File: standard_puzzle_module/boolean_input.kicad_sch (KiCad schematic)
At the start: 6 parts, among them J8 Screw_Terminal_01x02, U8 PC817

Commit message: feat: unscrew git tracking
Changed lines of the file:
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@@
+	(wire
+		(pts
+			(xy 166.37 90.17) (xy 172.72 90.17)
+		)
+		(stroke
+			(width 0)
+			(type default)
+		)
+	)
 	(wire
 		(pts
@@
 				(justify left)
 			)
+		)
+	)
+	(hierarchical_label "in"
+		(shape output)
+		(at 172.72 90.17 0)
+		(effects
+			(font
+				(size 1.27 1.27)
+			)
+			(justify left)
 		)
 	)
@@
 		(instances
 			(project "standard_puzzle_box"
+				(path "/13314f97-080e-4924-a8fe-b4d224920625/30374950-90da-411c-8e4a-5ea850107fc3"
+					(reference "R25")
+					(unit 1)
+				)
 				(path "/13314f97-080e-4924-a8fe-b4d224920625/5f64ce72-3807-4d88-a28a-0ca03d044e7a"
 					(reference "R17")
+					(unit 1)
+				)
+				(path "/13314f97-080e-4924-a8fe-b4d224920625/e263c93f-c5f2-4128-9ed9-7224d6818bb3"
+					(reference "R24")
+					(unit 1)
+				)
+				(path "/13314f97-080e-4924-a8fe-b4d224920625/e6ebc0cf-0436-4396-9996-34f92e1726df"
+					(reference "R23")
 					(unit 1)
 				)
@@
 		(instances
 			(project "standard_puzzle_box"
+				(path "/13314f97-080e-4924-a8fe-b4d224920625/30374950-90da-411c-8e4a-5ea850107fc3"
+					(reference "D18")
+					(unit 1)
+				)
 				(path "/13314f97-080e-4924-a8fe-b4d224920625/5f64ce72-3807-4d88-a28a-0ca03d044e7a"
 					(reference "D8")
+					(unit 1)
+				)
+				(path "/13314f97-080e-4924-a8fe-b4d224920625/e263c93f-c5f2-4128-9ed9-7224d6818bb3"
+					(reference "D17")
+					(unit 1)
+				)
+				(path "/13314f97-080e-4924-a8fe-b4d224920625/e6ebc0cf-0436-4396-9996-34f92e1726df"
+					(reference "D16")
 					(unit 1)
 				)
@@
 		(instances
 			(project "standard_puzzle_box"
+				(path "/13314f97-080e-4924-a8fe-b4d224920625/30374950-90da-411c-8e4a-5ea850107fc3"
+					(reference "J15")
+					(unit 1)
+				)
 				(path "/13314f97-080e-4924-a8fe-b4d224920625/5f64ce72-3807-4d88-a28a-0ca03d044e7a"
 					(reference "J8")
+					(unit 1)
+				)
+				(path "/13314f97-080e-4924-a8fe-b4d224920625/e263c93f-c5f2-4128-9ed9-7224d6818bb3"
+					(reference "J14")
+					(unit 1)
+				)
+				(path "/13314f97-080e-4924-a8fe-b4d224920625/e6ebc0cf-0436-4396-9996-34f92e1726df"
+					(reference "J13")
 					(unit 1)
 				)
@@
 		(instances
 			(project "standard_puzzle_box"
+				(path "/13314f97-080e-4924-a8fe-b4d224920625/30374950-90da-411c-8e4a-5ea850107fc3"
+					(reference "#PWR069")
+					(unit 1)
+				)
 				(path "/13314f97-080e-4924-a8fe-b4d224920625/5f64ce72-3807-4d88-a28a-0ca03d044e7a"
 					(reference "#PWR038")
+					(unit 1)
+				)
+				(path "/13314f97-080e-4924-a8fe-b4d224920625/e263c93f-c5f2-4128-9ed9-7224d6818bb3"
+					(reference "#PWR065")
+					(unit 1)
+				)
+				(path "/13314f97-080e-4924-a8fe-b4d224920625/e6ebc0cf-0436-4396-9996-34f92e1726df"
+					(reference "#PWR061")
 					(unit 1)
 				)
@@
 		(instances
 			(project "standard_puzzle_box"
+				(path "/13314f97-080e-4924-a8fe-b4d224920625/30374950-90da-411c-8e4a-5ea850107fc3"
+					(reference "#PWR070")
+					(unit 1)
+				)
 				(path "/13314f97-080e-4924-a8fe-b4d224920625/5f64ce72-3807-4d88-a28a-0ca03d044e7a"
 					(reference "#PWR039")
+					(unit 1)
+				)
+				(path "/13314f97-080e-4924-a8fe-b4d224920625/e263c93f-c5f2-4128-9ed9-7224d6818bb3"
+					(reference "#PWR066")
+					(unit 1)
+				)
+				(path "/13314f97-080e-4924-a8fe-b4d224920625/e6ebc0cf-0436-4396-9996-34f92e1726df"
+					(reference "#PWR062")
 					(unit 1)
 				)
@@
 		(instances
 			(project "standard_puzzle_box"
+				(path "/13314f97-080e-4924-a8fe-b4d224920625/30374950-90da-411c-8e4a-5ea850107fc3"
+					(reference "C20")
+					(unit 1)
+				)
 				(path "/13314f97-080e-4924-a8fe-b4d224920625/5f64ce72-3807-4d88-a28a-0ca03d044e7a"
 					(reference "C12")
+					(unit 1)
+				)
+				(path "/13314f97-080e-4924-a8fe-b4d224920625/e263c93f-c5f2-4128-9ed9-7224d6818bb3"
+					(reference "C19")
+					(unit 1)
+				)
+				(path "/13314f97-080e-4924-a8fe-b4d224920625/e6ebc0cf-0436-4396-9996-34f92e1726df"
+					(reference "C18")
 					(unit 1)
 				)
@@
 		(instances
 			(project "standard_puzzle_box"
+				(path "/13314f97-080e-4924-a8fe-b4d224920625/30374950-90da-411c-8e4a-5ea850107fc3"
+					(reference "#PWR071")
+					(unit 1)
+				)
 				(path "/13314f97-080e-4924-a8fe-b4d224920625/5f64ce72-3807-4d88-a28a-0ca03d044e7a"
 					(reference "#PWR040")
+					(unit 1)
+				)
+				(path "/13314f97-080e-4924-a8fe-b4d224920625/e263c93f-c5f2-4128-9ed9-7224d6818bb3"
+					(reference "#PWR067")
+					(unit 1)
+				)
+				(path "/13314f97-080e-4924-a8fe-b4d224920625/e6ebc0cf-0436-4396-9996-34f92e1726df"
+					(reference "#PWR063")
 					(unit 1)
 				)
@@
 		(instances
 			(project "standard_puzzle_box"
+				(path "/13314f97-080e-4924-a8fe-b4d224920625/30374950-90da-411c-8e4a-5ea850107fc3"
+					(reference "R13")
+					(unit 1)
+				)
 				(path "/13314f97-080e-4924-a8fe-b4d224920625/5f64ce72-3807-4d88-a28a-0ca03d044e7a"
 					(reference "R10")
+					(unit 1)
+				)
+				(path "/13314f97-080e-4924-a8fe-b4d224920625/e263c93f-c5f2-4128-9ed9-7224d6818bb3"
+					(reference "R12")
+					(unit 1)
+				)
+				(path "/13314f97-080e-4924-a8fe-b4d224920625/e6ebc0cf-0436-4396-9996-34f92e1726df"
+					(reference "R11")
 					(unit 1)
 				)
@@
 		(instances
 			(project "standard_puzzle_box"
+				(path "/13314f97-080e-4924-a8fe-b4d224920625/30374950-90da-411c-8e4a-5ea850107fc3"
+					(reference "#PWR08")
+					(unit 1)
+				)
 				(path "/13314f97-080e-4924-a8fe-b4d224920625/5f64ce72-3807-4d88-a28a-0ca03d044e7a"
 					(reference "#PWR03")
+					(unit 1)
+				)
+				(path "/13314f97-080e-4924-a8fe-b4d224920625/e263c93f-c5f2-4128-9ed9-7224d6818bb3"
+					(reference "#PWR06")
+					(unit 1)
+				)
+				(path "/13314f97-080e-4924-a8fe-b4d224920625/e6ebc0cf-0436-4396-9996-34f92e1726df"
+					(reference "#PWR05")
 					(unit 1)
 				)
@@
 		(instances
 			(project "standard_puzzle_box"
+				(path "/13314f97-080e-4924-a8fe-b4d224920625/30374950-90da-411c-8e4a-5ea850107fc3"
+					(reference "#PWR072")
+					(unit 1)
+				)
 				(path "/13314f97-080e-4924-a8fe-b4d224920625/5f64ce72-3807-4d88-a28a-0ca03d044e7a"
 					(reference "#PWR041")
+					(unit 1)
+				)
+				(path "/13314f97-080e-4924-a8fe-b4d224920625/e263c93f-c5f2-4128-9ed9-7224d6818bb3"
+					(reference "#PWR068")
+					(unit 1)
+				)
+				(path "/13314f97-080e-4924-a8fe-b4d224920625/e6ebc0cf-0436-4396-9996-34f92e1726df"
+					(reference "#PWR064")
 					(unit 1)
 				)
@@
 		(instances
 			(project "standard_puzzle_box"
+				(path "/13314f97-080e-4924-a8fe-b4d224920625/30374950-90da-411c-8e4a-5ea850107fc3"
+					(reference "U12")
+					(unit 1)
+				)
 				(path "/13314f97-080e-4924-a8fe-b4d224920625/5f64ce72-3807-4d88-a28a-0ca03d044e7a"
 					(reference "U8")
 					(unit 1)
 				)
+				(path "/13314f97-080e-4924-a8fe-b4d224920625/e263c93f-c5f2-4128-9ed9-7224d6818bb3"
+					(reference "U11")
+					(unit 1)
+				)
+				(path "/13314f97-080e-4924-a8fe-b4d224920625/e6ebc0cf-0436-4396-9996-34f92e1726df"
+					(reference "U10")
+					(unit 1)
+				)

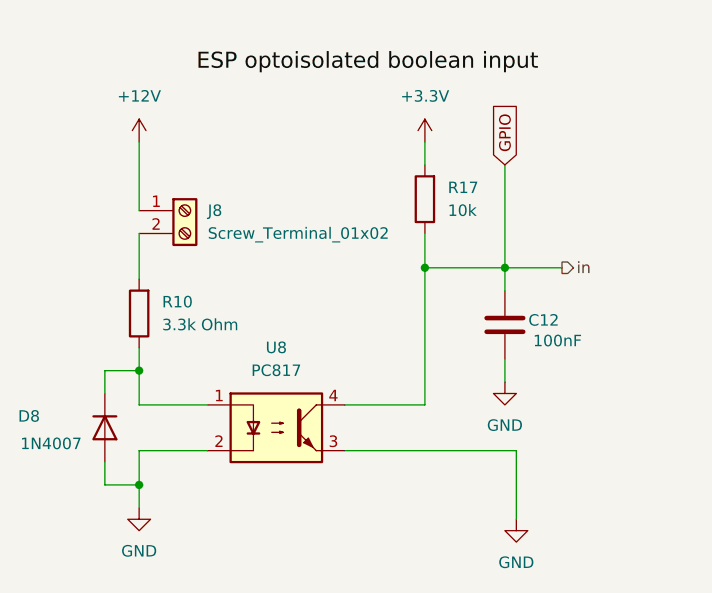
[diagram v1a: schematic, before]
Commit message: feat: clean up schematic references and run clean annotation
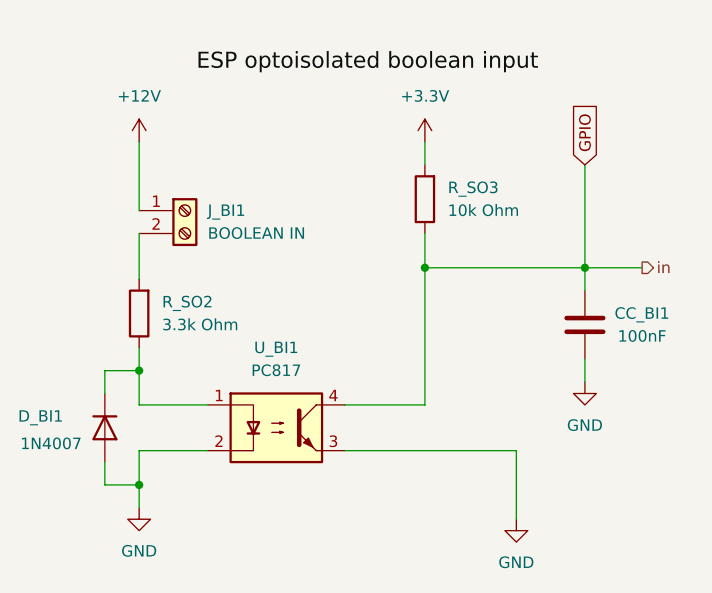
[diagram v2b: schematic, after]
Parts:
- CC_BI1: renamed from C12; footprint (none) -> Capacitor_THT:C_Disc_D5.0mm_W2.5mm_P5.00mm
- J_BI1: renamed from J8; value Screw_Terminal_01x02 -> BOOLEAN IN; footprint (none) -> TerminalBlock_Phoenix:TerminalBlock_Phoenix_MKDS-1,5-2-5.08_1x02_P5.08mm_Horizontal
- R_SO2: renamed from R10; footprint (none) -> Resistor_THT:R_Axial_DIN0411_L9.9mm_D3.6mm_P15.24mm_Horizontal
- R_SO3: renamed from R17; value 10k -> 10k Ohm; footprint (none) -> Resistor_THT:R_Axial_DIN0411_L9.9mm_D3.6mm_P15.24mm_Horizontal
- renumbered D8 to D_BI1, U8 to U_BI1
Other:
- moved on the sheet: CC_BI1

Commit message: fix: run erc and fix errors and warnings
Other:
- note added: "ESP optoisolated boolean input"
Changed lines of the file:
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@@
 		(title "ESP optoisolated boolean input")
 	)
-	(junction
-		(at 175.26 90.17)
-		(diameter 0)
-		(color 0 0 0 0)
-	)
-	(junction
-		(at 125.73 114.3)
-		(diameter 0)
-		(color 0 0 0 0)
-	)
-	(junction
-		(at 125.73 101.6)
-		(diameter 0)
-		(color 0 0 0 0)
-	)
-	(junction
-		(at 157.48 90.17)
-		(diameter 0)
-		(color 0 0 0 0)
-	)
-	(wire
-		(pts
-			(xy 175.26 78.74) (xy 175.26 90.17)
-		)
-		(stroke
-			(width 0)
-			(type default)
-		)
-	)
-	(wire
-		(pts
-			(xy 175.26 100.33) (xy 175.26 102.87)
-		)
-		(stroke
-			(width 0)
-			(type default)
-		)
-	)
-	(wire
-		(pts
-			(xy 157.48 86.36) (xy 157.48 90.17)
-		)
-		(stroke
-			(width 0)
-			(type default)
-		)
-	)
-	(wire
-		(pts
-			(xy 125.73 76.2) (xy 125.73 83.82)
-		)
-		(stroke
-			(width 0)
-			(type default)
-		)
-	)
-	(wire
-		(pts
-			(xy 121.92 114.3) (xy 125.73 114.3)
-		)
-		(stroke
-			(width 0)
-			(type default)
-		)
-	)
-	(wire
-		(pts
-			(xy 157.48 105.41) (xy 157.48 90.17)
-		)
-		(stroke
-			(width 0)
-			(type default)
-		)
-	)
-	(wire
-		(pts
-			(xy 125.73 110.49) (xy 125.73 114.3)
-		)
-		(stroke
-			(width 0)
-			(type default)
-		)
-	)
-	(wire
-		(pts
-			(xy 133.35 110.49) (xy 125.73 110.49)
-		)
-		(stroke
-			(width 0)
-			(type default)
-		)
-	)
-	(wire
-		(pts
-			(xy 175.26 90.17) (xy 181.61 90.17)
-		)
-		(stroke
-			(width 0)
-			(type default)
-		)
-	)
-	(wire
-		(pts
-			(xy 167.64 110.49) (xy 167.64 118.11)
-		)
-		(stroke
-			(width 0)
-			(type default)
-		)
-	)
-	(wire
-		(pts
-			(xy 125.73 101.6) (xy 125.73 105.41)
-		)
-		(stroke
-			(width 0)
-			(type default)
-		)
-	)
-	(wire
-		(pts
-			(xy 157.48 76.2) (xy 157.48 78.74)
-		)
-		(stroke
-			(width 0)
-			(type default)
-		)
-	)
-	(wire
-		(pts
-			(xy 148.59 105.41) (xy 157.48 105.41)
-		)
-		(stroke
-			(width 0)
-			(type default)
-		)
-	)
-	(wire
-		(pts
-			(xy 121.92 101.6) (xy 125.73 101.6)
-		)
-		(stroke
-			(width 0)
-			(type default)
-		)
-	)
-	(wire
-		(pts
-			(xy 121.92 111.76) (xy 121.92 114.3)
-		)
-		(stroke
-			(width 0)
-			(type default)
-		)
-	)
-	(wire
-		(pts
-			(xy 125.73 105.41) (xy 133.35 105.41)
-		)
-		(stroke
-			(width 0)
-			(type default)
-		)
-	)
-	(wire
-		(pts
-			(xy 125.73 114.3) (xy 125.73 116.84)
-		)
-		(stroke
-			(width 0)
-			(type default)
-		)
-	)
-	(wire
-		(pts
-			(xy 125.73 86.36) (xy 125.73 91.44)
-		)
-		(stroke
-			(width 0)
-			(type default)
-		)
-	)
-	(wire
-		(pts
-			(xy 125.73 99.06) (xy 125.73 101.6)
-		)
-		(stroke
-			(width 0)
-			(type default)
-		)
-	)
-	(wire
-		(pts
-			(xy 157.48 90.17) (xy 175.26 90.17)
-		)
-		(stroke
-			(width 0)
-			(type default)
-		)
-	)
-	(wire
-		(pts
-			(xy 175.26 90.17) (xy 175.26 92.71)
-		)
-		(stroke
-			(width 0)
-			(type default)
-		)
-	)
-	(wire
-		(pts
-			(xy 148.59 110.49) (xy 167.64 110.49)
-		)
-		(stroke
-			(width 0)
-			(type default)
-		)
-	)
-	(wire
-		(pts
-			(xy 121.92 104.14) (xy 121.92 101.6)
-		)
-		(stroke
-			(width 0)
-			(type default)
-		)
-	)
-	(label "ESP optoisolated boolean input"
-		(at 132.08 68.58 0)
+	(text "ESP optoisolated boolean input"
+		(exclude_from_sim no)
+		(at 124.46 64.77 0)
 		(effects
 			(font
-				(size 1.778 1.778)
+				(size 2.032 2.032)
+				(color 255 97 9 1)
 			)
-			(justify left bottom)
+			(justify left)
+		)
+	)
+	(junction
+		(at 175.26 90.17)
+		(diameter 0)
+		(color 0 0 0 0)
+	)
+	(junction
+		(at 125.73 114.3)
+		(diameter 0)
+		(color 0 0 0 0)
+	)
+	(junction
+		(at 125.73 101.6)
+		(diameter 0)
+		(color 0 0 0 0)
+	)
+	(junction
+		(at 157.48 90.17)
+		(diameter 0)
+		(color 0 0 0 0)
+	)
+	(wire
+		(pts
+			(xy 175.26 78.74) (xy 175.26 90.17)
+		)
+		(stroke
+			(width 0)
+			(type default)
+		)
+	)
+	(wire
+		(pts
+			(xy 175.26 100.33) (xy 175.26 102.87)
+		)
+		(stroke
+			(width 0)
+			(type default)
+		)
+	)
+	(wire
+		(pts
+			(xy 157.48 86.36) (xy 157.48 90.17)
+		)
+		(stroke
+			(width 0)
+			(type default)
+		)
+	)
+	(wire
+		(pts
+			(xy 125.73 76.2) (xy 125.73 83.82)
+		)
+		(stroke
+			(width 0)
+			(type default)
+		)
+	)
+	(wire
+		(pts
+			(xy 121.92 114.3) (xy 125.73 114.3)
+		)
+		(stroke
+			(width 0)
+			(type default)
+		)
+	)
+	(wire
+		(pts
+			(xy 157.48 105.41) (xy 157.48 90.17)
+		)
+		(stroke
+			(width 0)
+			(type default)
+		)
+	)
+	(wire
+		(pts
+			(xy 125.73 110.49) (xy 125.73 114.3)
+		)
+		(stroke
+			(width 0)
+			(type default)
+		)
+	)
+	(wire
+		(pts
+			(xy 133.35 110.49) (xy 125.73 110.49)
+		)
+		(stroke
+			(width 0)
+			(type default)
+		)
+	)
+	(wire
+		(pts
+			(xy 175.26 90.17) (xy 181.61 90.17)
+		)
+		(stroke
+			(width 0)
+			(type default)
+		)
+	)
+	(wire
+		(pts
+			(xy 167.64 110.49) (xy 167.64 118.11)
+		)
+		(stroke
+			(width 0)
+			(type default)
+		)
+	)
+	(wire
+		(pts
+			(xy 125.73 101.6) (xy 125.73 105.41)
+		)
+		(stroke
+			(width 0)
+			(type default)
+		)
+	)
+	(wire
+		(pts
+			(xy 157.48 76.2) (xy 157.48 78.74)
+		)
+		(stroke
+			(width 0)
+			(type default)
+		)
+	)
+	(wire
+		(pts
+			(xy 148.59 105.41) (xy 157.48 105.41)
+		)
+		(stroke
+			(width 0)
+			(type default)
+		)
+	)
+	(wire
+		(pts
+			(xy 121.92 101.6) (xy 125.73 101.6)
+		)
+		(stroke
+			(width 0)
+			(type default)
+		)
+	)
+	(wire
+		(pts
+			(xy 121.92 111.76) (xy 121.92 114.3)
+		)
+		(stroke
+			(width 0)
+			(type default)
+		)
+	)
+	(wire
+		(pts
+			(xy 125.73 105.41) (xy 133.35 105.41)
+		)
+		(stroke
+			(width 0)
+			(type default)
+		)
+	)
+	(wire
+		(pts
+			(xy 125.73 114.3) (xy 125.73 116.84)
+		)
+		(stroke
+			(width 0)
+			(type default)
+		)
+	)
+	(wire
+		(pts
+			(xy 125.73 86.36) (xy 125.73 91.44)
+		)
+		(stroke
+			(width 0)
+			(type default)
+		)
+	)
+	(wire
+		(pts
+			(xy 125.73 99.06) (xy 125.73 101.6)
+		)
+		(stroke
+			(width 0)
+			(type default)
+		)
+	)
+	(wire
+		(pts
+			(xy 157.48 90.17) (xy 175.26 90.17)
+		)
+		(stroke
+			(width 0)
+			(type default)
+		)
+	)
+	(wire
+		(pts
+			(xy 175.26 90.17) (xy 175.26 92.71)
+		)
+		(stroke
+			(width 0)
+			(type default)
+		)
+	)
+	(wire
+		(pts
+			(xy 148.59 110.49) (xy 167.64 110.49)
+		)
+		(stroke
+			(width 0)
+			(type default)
+		)
+	)
+	(wire
+		(pts
+			(xy 121.92 104.14) (xy 121.92 101.6)
+		)
+		(stroke
+			(width 0)
+			(type default)
 		)
 	)
@@
 		)
 	)
-	(hierarchical_label "in"
+	(hierarchical_label "out"
 		(shape output)
 		(at 181.61 90.17 0)

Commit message: feat: dump working files before blackout
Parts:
- R_SO2: value 3.3k Ohm -> 3.3k
- R_SO3: value 10k Ohm -> 10k
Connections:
- net GPIO renamed out
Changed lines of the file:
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@@
-	(wire
-		(pts
-			(xy 175.26 78.74) (xy 175.26 90.17)
-		)
-		(stroke
-			(width 0)
-			(type default)
-		)
-	)
 	(wire
 		(pts
@@
 			(width 0)
 			(type default)
-		)
-	)
-	(global_label "GPIO"
-		(shape input)
-		(at 175.26 78.74 90)
-		(fields_autoplaced yes)
-		(effects
-			(font
-				(size 1.27 1.27)
-			)
-			(justify left)
-		)
-		(property "Intersheetrefs" "${INTERSHEET_REFS}"
-			(at 175.26 71.2795 90)
-			(hide yes)
-			(show_name no)
-			(do_not_autoplace no)
-			(effects
-				(font
-					(size 1.27 1.27)
-				)
-				(justify left)
-			)
 		)
 	)
@@
 			)
 		)
-		(property "Value" "10k Ohm"
+		(property "Value" "10k"
 			(at 160.02 83.8199 0)
 			(show_name no)
@@
 			)
 		)
-		(property "Value" "3.3k Ohm"
+		(property "Value" "3.3k"
 			(at 128.27 96.5199 0)
 			(show_name no)

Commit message: fix: block reverse current in BO block rather than lead it to gnd
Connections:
- net GND: no longer D_BI1.2 (A)
- net at D_BI1.1 (K), U_BI1.1: no longer R_SO2.1
- new net: D_BI1.2 (A), R_SO2.1
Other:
- moved on the sheet: D_BI1, J_BI1, R_SO2
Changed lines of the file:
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@@
-	)
-	(junction
-		(at 125.73 114.3)
-		(diameter 0)
-		(color 0 0 0 0)
-	)
-	(junction
-		(at 125.73 101.6)
-		(diameter 0)
-		(color 0 0 0 0)
 	)
 	(junction
@@
 	(wire
 		(pts
-			(xy 125.73 76.2) (xy 125.73 83.82)
-		)
-		(stroke
-			(width 0)
-			(type default)
-		)
-	)
-	(wire
-		(pts
-			(xy 121.92 114.3) (xy 125.73 114.3)
+			(xy 125.73 76.2) (xy 125.73 80.01)
+		)
+		(stroke
+			(width 0)
+			(type default)
+		)
+	)
+	(wire
+		(pts
+			(xy 133.35 105.41) (xy 125.73 105.41)
+		)
+		(stroke
+			(width 0)
+			(type default)
+		)
+	)
+	(wire
+		(pts
+			(xy 125.73 92.71) (xy 125.73 95.25)
 		)
 		(stroke
@@
 	(wire
 		(pts
-			(xy 125.73 110.49) (xy 125.73 114.3)
+			(xy 125.73 110.49) (xy 125.73 116.84)
 		)
 		(stroke
@@
 	(wire
 		(pts
-			(xy 125.73 101.6) (xy 125.73 105.41)
+			(xy 125.73 105.41) (xy 125.73 102.87)
 		)
 		(stroke
@@
 	(wire
 		(pts
-			(xy 121.92 101.6) (xy 125.73 101.6)
-		)
-		(stroke
-			(width 0)
-			(type default)
-		)
-	)
-	(wire
-		(pts
-			(xy 121.92 111.76) (xy 121.92 114.3)
-		)
-		(stroke
-			(width 0)
-			(type default)
-		)
-	)
-	(wire
-		(pts
-			(xy 125.73 105.41) (xy 133.35 105.41)
-		)
-		(stroke
-			(width 0)
-			(type default)
-		)
-	)
-	(wire
-		(pts
-			(xy 125.73 114.3) (xy 125.73 116.84)
-		)
-		(stroke
-			(width 0)
-			(type default)
-		)
-	)
-	(wire
-		(pts
-			(xy 125.73 86.36) (xy 125.73 91.44)
-		)
-		(stroke
-			(width 0)
-			(type default)
-		)
-	)
-	(wire
-		(pts
-			(xy 125.73 99.06) (xy 125.73 101.6)
+			(xy 125.73 82.55) (xy 125.73 85.09)
 		)
 		(stroke
@@
 		(pts
 			(xy 148.59 110.49) (xy 167.64 110.49)
-		)
-		(stroke
-			(width 0)
-			(type default)
-		)
-	)
-	(wire
-		(pts
-			(xy 121.92 104.14) (xy 121.92 101.6)
 		)
 		(stroke
@@
 	(symbol
 		(lib_id "Diode:1N4007")
-		(at 121.92 107.95 270)
+		(at 125.73 99.06 90)
 		(unit 1)
 		(body_style 1)
@@
 		(dnp no)
 		(property "Reference" "D_BI1"
-			(at 112.268 106.68 90)
+			(at 135.382 100.33 90)
 			(show_name no)
 			(do_not_autoplace no)
@@
 		)
 		(property "Value" "1N4007"
-			(at 112.522 109.728 90)
+			(at 135.128 97.282 90)
 			(show_name no)
 			(do_not_autoplace no)
@@
 		)
 		(property "Footprint" "Diode_THT:D_DO-41_SOD81_P10.16mm_Horizontal"
-			(at 117.475 107.95 0)
+			(at 130.175 99.06 0)
 			(hide yes)
 			(show_name no)
@@
 		)
 		(property "Datasheet" "http://www.vishay.com/docs/88503/1n4001.pdf"
-			(at 121.92 107.95 0)
+			(at 125.73 99.06 0)
 			(hide yes)
 			(show_name no)
@@
 		)
 		(property "Description" "1000V 1A General Purpose Rectifier Diode, DO-41"
-			(at 121.92 107.95 0)
+			(at 125.73 99.06 0)
 			(hide yes)
 			(show_name no)
@@
 		)
 		(property "Sim.Device" "D"
-			(at 121.92 107.95 0)
+			(at 125.73 99.06 0)
 			(hide yes)
 			(show_name no)
@@
 		)
 		(property "Sim.Pins" "1=K 2=A"
-			(at 121.92 107.95 0)
+			(at 125.73 99.06 0)
 			(hide yes)
 			(show_name no)
@@
 	(symbol
 		(lib_id "Connector:Screw_Terminal_01x02")
-		(at 130.81 83.82 0)
+		(at 130.81 80.01 0)
 		(unit 1)
 		(body_style 1)
@@
 		(fields_autoplaced yes)
 		(property "Reference" "J_BI1"
-			(at 133.35 83.8199 0)
+			(at 133.35 80.0099 0)
 			(show_name no)
 			(do_not_autoplace no)
@@
 		)
 		(property "Value" "BOOLEAN IN"
-			(at 133.35 86.3599 0)
+			(at 133.35 82.5499 0)
 			(show_name no)
 			(do_not_autoplace no)
@@
 		)
 		(property "Footprint" "TerminalBlock_Phoenix:TerminalBlock_Phoenix_MKDS-1,5-2-5.08_1x02_P5.08mm_Horizontal"
-			(at 130.81 83.82 0)
+			(at 130.81 80.01 0)
 			(hide yes)
 			(show_name no)
@@
 		)
 		(property "Datasheet" ""
-			(at 130.81 83.82 0)
+			(at 130.81 80.01 0)
 			(hide yes)
 			(show_name no)
@@
 		)
 		(property "Description" "Generic screw terminal, single row, 01x02, script generated (kicad-library-utils/schlib/autogen/connector/)"
-			(at 130.81 83.82 0)
+			(at 130.81 80.01 0)
 			(hide yes)
 			(show_name no)
@@
 	(symbol
 		(lib_id "Device:R")
-		(at 125.73 95.25 180)
+		(at 125.73 88.9 180)
 		(unit 1)
 		(body_style 1)
@@
 		(fields_autoplaced yes)
 		(property "Reference" "R_SO2"
-			(at 128.27 93.9799 0)
+			(at 128.27 87.6299 0)
 			(show_name no)
 			(do_not_autoplace no)
@@
 		)
 		(property "Value" "3.3k"
-			(at 128.27 96.5199 0)
+			(at 128.27 90.1699 0)
 			(show_name no)
 			(do_not_autoplace no)
@@
 		)
 		(property "Footprint" "Resistor_THT:R_Axial_DIN0411_L9.9mm_D3.6mm_P15.24mm_Horizontal"
-			(at 127.508 95.25 90)
+			(at 127.508 88.9 90)
 			(hide yes)
 			(show_name no)
@@
 		)
 		(property "Datasheet" ""
-			(at 125.73 95.25 0)
+			(at 125.73 88.9 0)
 			(hide yes)
 			(show_name no)
@@
 		)
 		(property "Description" "Resistor"
-			(at 125.73 95.25 0)
-			(hide yes)
-			(show_name no)
+			(at 125.73 88.9 0)
+			(hide yes)
+			(show_name no)

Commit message: feat: salvaging stuff after lossy crash
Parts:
- R_SO2, R_SO3: footprint Resistor_THT:R_Axial_DIN0411_L9.9mm_D3.6mm_P15.24mm_Horizontal -> Resistor_THT:R_Axial_DIN0207_L6.3mm_D2.5mm_P10.16mm_Horizontal
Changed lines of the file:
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@@
 			)
 		)
-		(property "Footprint" "Resistor_THT:R_Axial_DIN0411_L9.9mm_D3.6mm_P15.24mm_Horizontal"
+		(property "Footprint" "Resistor_THT:R_Axial_DIN0207_L6.3mm_D2.5mm_P10.16mm_Horizontal"
 			(at 159.258 82.55 90)
 			(hide yes)
@@
 			)
 		)
-		(property "Footprint" "Resistor_THT:R_Axial_DIN0411_L9.9mm_D3.6mm_P15.24mm_Horizontal"
+		(property "Footprint" "Resistor_THT:R_Axial_DIN0207_L6.3mm_D2.5mm_P10.16mm_Horizontal"
 			(at 127.508 88.9 90)
 			(hide yes)
